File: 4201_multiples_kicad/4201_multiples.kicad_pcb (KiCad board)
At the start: 4 copper layers, 60 x 110 mm, 42 parts, among them J1 Conn_02x05_Odd_Even, J2 PJ398SM, J3 PJ398SM, J4 PJ398SM, J5 PJ398SM, J6 PJ398SM, J7 PJ398SM, J8 PJ398SM, J9 PJ398SM, U1 TL074, U2 TL074

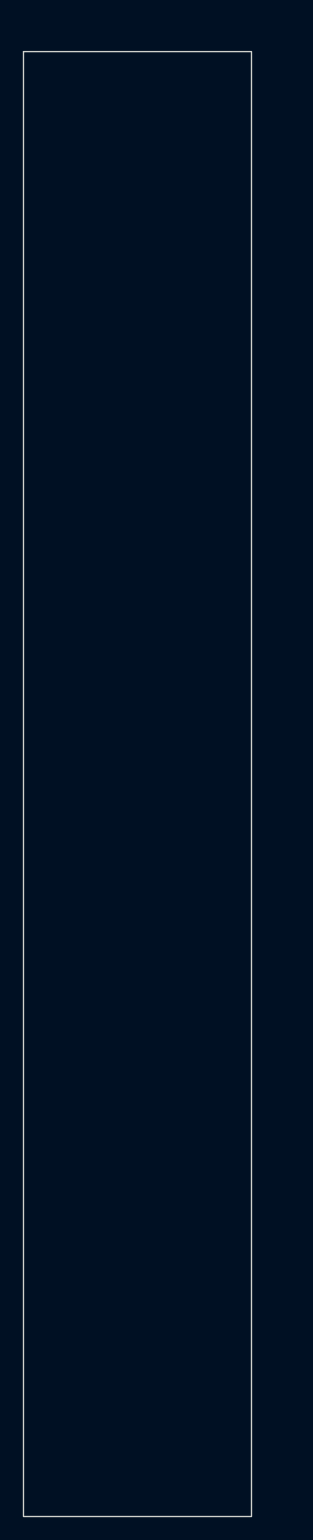
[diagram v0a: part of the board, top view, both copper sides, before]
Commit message: Add front panel silk footprint
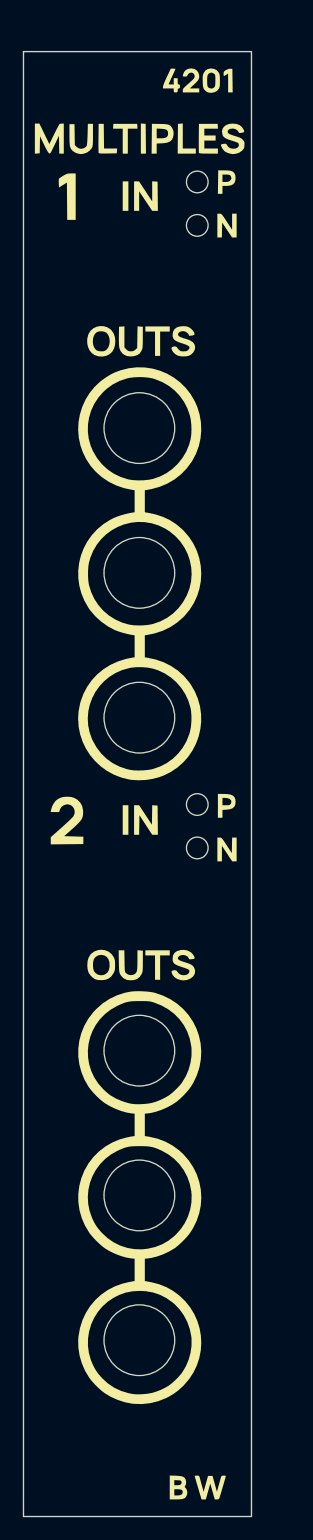
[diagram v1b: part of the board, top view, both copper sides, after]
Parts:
- added G***: LOGO, 4201_multiples:4204_multiples_panel_silk, F.Cu at (52.2, 41.5)
- added REF**: PJ392_Drill_Hole_Panel, OS_Drill_Holes:PJ392_Drill_Hole_Panel_D6.2mm, F.Cu at (50.2, 73.0)
- added REF**: Hole_1.9mm_LED, OS_Drill_Holes:LED_1.8mm_Drill_Hole_Panel_D1.9mm, F.Cu at (55.2, 55.2)
- added REF**: PJ392_Drill_Hole_Panel, OS_Drill_Holes:PJ392_Drill_Hole_Panel_D6.2mm, F.Cu at (50.2, 98.4)
- added REF**: Hole_1.9mm_LED, OS_Drill_Holes:LED_1.8mm_Drill_Hole_Panel_D1.9mm, F.Cu at (55.2, 51.4)
- added REF**: PJ392_Drill_Hole_Panel, OS_Drill_Holes:PJ392_Drill_Hole_Panel_D6.2mm, F.Cu at (50.2, 153.0)
- added REF**: PJ392_Drill_Hole_Panel, OS_Drill_Holes:PJ392_Drill_Hole_Panel_D6.2mm, F.Cu at (50.2, 127.6)
- added REF**: PJ392_Drill_Hole_Panel, OS_Drill_Holes:PJ392_Drill_Hole_Panel_D6.2mm, F.Cu at (50.2, 140.3)
- added REF**: PJ392_Drill_Hole_Panel, OS_Drill_Holes:PJ392_Drill_Hole_Panel_D6.2mm, F.Cu at (50.2, 85.7)
- added REF**: Hole_1.9mm_LED, OS_Drill_Holes:LED_1.8mm_Drill_Hole_Panel_D1.9mm, F.Cu at (55.2, 109.9)
- added REF**: Hole_1.9mm_LED, OS_Drill_Holes:LED_1.8mm_Drill_Hole_Panel_D1.9mm, F.Cu at (55.2, 106.0)

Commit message: Continue work on PCB layouts
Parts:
- removed the REF** at (50.2, 73.0)
- removed the REF** at (55.2, 55.2)
- removed the REF** at (50.2, 98.4)
- removed the REF** at (55.2, 51.4)
- removed the REF** at (50.2, 153.0)
- removed the REF** at (50.2, 127.6)
- removed the REF** at (50.2, 140.3)
- removed the REF** at (50.2, 85.7)
- removed the REF** at (55.2, 109.9)
- removed the REF** at (55.2, 106.0)
- added J10: Conn_01x03_Female, Connector_PinSocket_2.54mm:PinSocket_1x03_P2.54mm_Vertical, B.Cu at (98.4, 62.2)
- added J11: Conn_01x04_Female, Connector_PinSocket_2.54mm:PinSocket_1x04_P2.54mm_Vertical, B.Cu at (83.2, 149.9)
- added J12: Conn_01x03_Female, Connector_PinSocket_2.54mm:PinSocket_1x03_P2.54mm_Vertical, B.Cu at (98.4, 144.8)
- added J13: Conn_01x05_Male, Connector_PinHeader_2.54mm:PinHeader_1x05_P2.54mm_Vertical, F.Cu at (123.2, 52.1)
- added J14: Conn_01x03_Male, Connector_PinHeader_2.54mm:PinHeader_1x03_P2.54mm_Vertical, F.Cu at (138.4, 62.2)
- added J15: Conn_01x04_Male, Connector_PinHeader_2.54mm:PinHeader_1x04_P2.54mm_Vertical, F.Cu at (123.2, 149.9)
- added J16: Conn_01x03_Male, Connector_PinHeader_2.54mm:PinHeader_1x03_P2.54mm_Vertical, F.Cu at (138.4, 144.8)
- added J17: Conn_02x05_Odd_Even, Connector_IDC:IDC-Header_2x05_P2.54mm_Vertical, B.Cu at (125.6, 111.1)
- added REF**: PJ392_Drill_Hole_Panel, OS_Drill_Holes:PJ392_Drill_Hole_Panel_D6.2mm, F.Cu at (50.8, 73.7)
- added REF**: Hole_M2.5_2.7mm, OS_Drill_Holes:M3_Drill_Hole_D3.2mm, F.Cu at (90.8, 92.7)
- added REF**: PJ392_Drill_Hole_Panel, OS_Drill_Holes:PJ392_Drill_Hole_Panel_D6.2mm, F.Cu at (50.8, 114.3)
- added REF**: Hole_1.9mm_LED, OS_Drill_Holes:LED_1.8mm_Drill_Hole_Panel_D1.9mm, F.Cu at (55.9, 106.7)
- added REF**: PJ392_Drill_Hole_Panel, OS_Drill_Holes:PJ392_Drill_Hole_Panel_D6.2mm, F.Cu at (50.8, 128.3)
- added REF**: Hole_1.9mm_LED, OS_Drill_Holes:LED_1.8mm_Drill_Hole_Panel_D1.9mm, F.Cu at (55.9, 110.5)
- added REF**: PJ392_Drill_Hole_Panel, OS_Drill_Holes:PJ392_Drill_Hole_Panel_D6.2mm, F.Cu at (50.8, 153.7)
- added REF**: Hole_1.9mm_LED, OS_Drill_Holes:LED_1.8mm_Drill_Hole_Panel_D1.9mm, F.Cu at (55.9, 52.1)
- added REF**: PJ392_Drill_Hole_Panel, OS_Drill_Holes:PJ392_Drill_Hole_Panel_D6.2mm, F.Cu at (50.8, 59.7)
- added REF**: PJ392_Drill_Hole_Panel, OS_Drill_Holes:PJ392_Drill_Hole_Panel_D6.2mm, F.Cu at (50.8, 141.0)
- added REF**: PJ392_Drill_Hole_Panel, OS_Drill_Holes:PJ392_Drill_Hole_Panel_D6.2mm, F.Cu at (50.8, 99.1)
- added REF**: Hole_M2.5_2.7mm, OS_Drill_Holes:M3_Drill_Hole_D3.2mm, F.Cu at (130.8, 92.7)
- added REF**: Hole_1.9mm_LED, OS_Drill_Holes:LED_1.8mm_Drill_Hole_Panel_D1.9mm, F.Cu at (55.9, 55.9)
- added REF**: PJ392_Drill_Hole_Panel, OS_Drill_Holes:PJ392_Drill_Hole_Panel_D6.2mm, F.Cu at (50.8, 86.4)
- C1, C2: moved to B.Cu
- D1, D3: value 1N4148 -> 1.8mm_green; footprint Diode_SMD:D_1206_3216Metric_Pad1.42x1.75mm_HandSolder -> LED_THT:LED_D1.8mm_W3.3mm_H2.4mm
- D10, D12: value 1.8mm_red -> 1N4148; footprint LED_THT:LED_D1.8mm_W3.3mm_H2.4mm -> Diode_SMD:D_1206_3216Metric_Pad1.42x1.75mm_HandSolder
- D11, D9: value 1.8mm_green -> 1N4148; footprint LED_THT:LED_D1.8mm_W3.3mm_H2.4mm -> Diode_SMD:D_1206_3216Metric_Pad1.42x1.75mm_HandSolder
- D2, D4: value 1N4148 -> 1.8mm_red; footprint Diode_SMD:D_1206_3216Metric_Pad1.42x1.75mm_HandSolder -> LED_THT:LED_D1.8mm_W3.3mm_H2.4mm
- J1: value Conn_02x05_Odd_Even -> AudioJack2; footprint Connector_IDC:IDC-Header_2x05_P2.54mm_Vertical -> OS_Connectors:Jack_3.5mm_PJ392_Vertical
- J2, J3, J4, J5, J6, J7, J8: value PJ398SM -> AudioJack2; footprint 4ms_Jack:EighthInch_PJ398SM -> OS_Connectors:Jack_3.5mm_PJ392_Vertical
- J9: value PJ398SM -> Conn_01x05_Female; footprint 4ms_Jack:EighthInch_PJ398SM -> Connector_PinSocket_2.54mm:PinSocket_1x05_P2.54mm_Vertical; moved to B.Cu
- R10, R12: value 4k7 -> 100R
- R11: value 39k -> 100R
- R2: value 220k -> 39k
- R3: value 100R -> 4k7
- R7: value 100R -> 220k
- R8: value 100R -> 39k
- R9: value 39k -> 4k7
- moved J7 187.8 mm to (90.8, 141.0)
- moved J8 173.8 mm to (90.8, 153.7)
- moved D3 167.1 mm to (94.6, 106.7)
- moved D10 165.7 mm to (134.0, 147.3)
- moved J5 161.2 mm to (90.8, 114.3)
- moved R9 158.6 mm to (145.4, 156.8)
- moved D1 154.7 mm to (94.6, 52.1)
- moved R12 152.9 mm to (149.2, 123.2), turned to 90 degrees
- moved J4 149.7 mm to (90.8, 99.1)
- moved D9 145.2 mm to (134.0, 144.8), turned to 180 degrees
- moved C2 144.8 mm to (136.5, 112.4), turned to -90 degrees
- moved D11 142.0 mm to (151.1, 154.3), turned to 180 degrees
- moved D4 140.3 mm to (97.2, 110.5), turned to 180 degrees
- moved D2 139.2 mm to (97.2, 55.9), turned to 180 degrees
- moved D12 135.0 mm to (151.1, 156.8)
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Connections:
- D1 pad 1: Net-(D1-Pad1) -> /interface/LED_1_PK_NA
- D1 pad 2: /U1D_FBK -> /interface/LED_1P_A
- D10 pad 1: Net-(D2-Pad2) -> /main_board/U2D_FBK
- D10 pad 2: /U1D_OUT -> /main_board/LED_2N_K
- D11 pad 1: /U2D_OUT -> GND
- D11 pad 2: Net-(D5-Pad1) -> Net-(D11-Pad2)
- D12 pad 1: Net-(D6-Pad2) -> Net-(D12-Pad1)
- D12 pad 2: /U2D_OUT -> GND
- D2 pad 1: /U1D_FBK -> /interface/LED_1N_K
- D2 pad 2: Net-(D2-Pad2) -> /interface/LED_1_PK_NA
- D3 pad 1: GND -> /interface/LED_2_PK_NA
- D3 pad 2: Net-(D3-Pad2) -> /interface/LED_2P_A
- D4 pad 1: Net-(D4-Pad1) -> /interface/LED_2N_K
- D4 pad 2: GND -> /interface/LED_2_PK_NA
- D5 pad 1: Net-(D5-Pad1) -> /main_board/LED_1P_A
- D5 pad 2: /U2D_FBK -> /main_board/U1D_FBK
- D6 pad 1: /U2D_FBK -> /main_board/U1D_FBK
- D6 pad 2: Net-(D6-Pad2) -> /main_board/LED_1N_K
- D9 pad 1: /U1D_OUT -> /main_board/LED_2P_A
- D9 pad 2: Net-(D1-Pad1) -> /main_board/U2D_FBK
- J9 pad 1: /OUT_2_3 -> /interface/IN_1
- J9 pad 2: GND -> /interface/OUT_1_1
- J9 pad 3: unconnected-(J9-Pad3) -> /interface/OUT_1_2
- R1 pad 2: /IN_1 -> /main_board/IN_1
- R10 pad 1: /U1D_FBK -> /main_board/U2A_OUT
- R10 pad 2: Net-(D4-Pad1) -> /main_board/OUT_2_1
- R11 pad 1: /U2D_FBK -> /main_board/U2B_OUT
- R11 pad 2: Net-(D7-Pad2) -> /main_board/OUT_2_2
- R12 pad 1: /U2D_FBK -> /main_board/U2C_OUT
- R12 pad 2: Net-(D8-Pad1) -> /main_board/OUT_2_3
- R2 pad 1: GND -> /main_board/U1D_FBK
- R2 pad 2: /IN_2 -> Net-(D7-Pad2)
- R3 pad 1: /U1A_OUT -> /main_board/U1D_FBK
- R3 pad 2: /OUT_1_1 -> Net-(D8-Pad1)
- R4 pad 1: /U1B_OUT -> /main_board/U1A_OUT
- R4 pad 2: /OUT_1_2 -> /main_board/OUT_1_1
- R5 pad 1: /U1C_OUT -> /main_board/U1B_OUT
- R5 pad 2: /OUT_1_3 -> /main_board/OUT_1_2
- R6 pad 1: /U2A_OUT -> /main_board/U1C_OUT
- R6 pad 2: /OUT_2_1 -> /main_board/OUT_1_3
- R7 pad 1: /U2B_OUT -> GND
- R7 pad 2: /OUT_2_2 -> /main_board/IN_2
- R8 pad 1: /U2C_OUT -> /main_board/U2D_FBK
- R8 pad 2: /OUT_2_3 -> Net-(D11-Pad2)
- R9 pad 1: /U1D_FBK -> /main_board/U2D_FBK
- R9 pad 2: Net-(D3-Pad2) -> Net-(D12-Pad1)
- U1 pad 1: /U1A_OUT -> /main_board/U1A_OUT
- U1 pad 10: /IN_1 -> /main_board/IN_1
- U1 pad 12: /IN_1 -> /main_board/IN_1
- U1 pad 13: /U1D_FBK -> /main_board/U1D_FBK
- U1 pad 14: /U1D_OUT -> /main_board/LED_1_PK_NA
- U1 pad 2: /U1A_OUT -> /main_board/U1A_OUT
- U1 pad 3: /IN_1 -> /main_board/IN_1
- U1 pad 5: /IN_1 -> /main_board/IN_1
- U1 pad 6: /U1B_OUT -> /main_board/U1B_OUT
- U1 pad 7: /U1B_OUT -> /main_board/U1B_OUT
- U1 pad 8: /U1C_OUT -> /main_board/U1C_OUT
- U1 pad 9: /U1C_OUT -> /main_board/U1C_OUT
- U2 pad 1: /U2A_OUT -> /main_board/U2A_OUT
- U2 pad 10: /IN_2 -> /main_board/IN_2
- U2 pad 12: /IN_2 -> /main_board/IN_2
- U2 pad 13: /U2D_FBK -> /main_board/U2D_FBK
- U2 pad 14: /U2D_OUT -> /main_board/LED_2_PK_NA
- U2 pad 2: /U2A_OUT -> /main_board/U2A_OUT
- U2 pad 3: /IN_2 -> /main_board/IN_2
- U2 pad 5: /IN_2 -> /main_board/IN_2
- U2 pad 6: /U2B_OUT -> /main_board/U2B_OUT
- U2 pad 7: /U2B_OUT -> /main_board/U2B_OUT
- U2 pad 8: /U2C_OUT -> /main_board/U2C_OUT
- U2 pad 9: /U2C_OUT -> /main_board/U2C_OUT
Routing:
- added copper zone on In1.Cu, net /interface/0V
- added copper zone on In2.Cu, net /interface/0V
- added copper zone on In1.Cu, net GND
- added copper zone on In2.Cu, net GND

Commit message: Layout components
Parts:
- added REF**: PinHeader_1x04_P2.54mm_Vertical, Connector_PinHeader_2.54mm:PinHeader_1x04_P2.54mm_Vertical, F.Cu at (126.9, 121.3)
- added REF**: PinSocket_1x04_P2.54mm_Vertical, Connector_PinSocket_2.54mm:PinSocket_1x04_P2.54mm_Vertical, B.Cu at (86.9, 121.3)
- C3, C4, C5, C6, D10, D11, D12, D5, D6, D7, D8, D9, R1, R10, R11, R12, R2, R3, R4, R5, R6, R7, R8, R9, U1, U2: moved to B.Cu
- moved R10 36.7 mm to (126.4, 138.4), turned to -90 degrees
- moved R6 36.2 mm to (128.9, 87.0), turned to 180 degrees
- moved C4 35.9 mm to (124.5, 81.3), turned to -90 degrees
- moved R7 33.1 mm to (130.8, 138.4), turned to 90 degrees
- moved R11 30.7 mm to (135.3, 138.4), turned to -90 degrees
- moved C5 30.5 mm to (124.5, 131.4), turned to 90 degrees
- moved R5 29.0 mm to (126.4, 74.3), turned to -90 degrees
- moved U1 28.6 mm to (130.8, 81.3), turned to 90 degrees
- moved U2 24.8 mm to (130.8, 131.4), turned to -90 degrees
- moved R1 22.9 mm to (130.8, 74.3), turned to -90 degrees
- moved C3 22.7 mm to (137.2, 81.3), turned to -90 degrees
- moved C6 21.5 mm to (137.2, 131.4), turned to 90 degrees
- moved R4 17.9 mm to (135.3, 74.3), turned to 90 degrees
- moved D11 16.4 mm to (134.7, 153.9)
- moved R8 16.4 mm to (129.0, 153.9)
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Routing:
- removed copper zone on In1.Cu, net /interface/0V
- removed copper zone on In2.Cu, net /interface/0V
- removed copper zone on In1.Cu, net GND
- removed copper zone on In2.Cu, net GND
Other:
- copper layers 4 -> 2

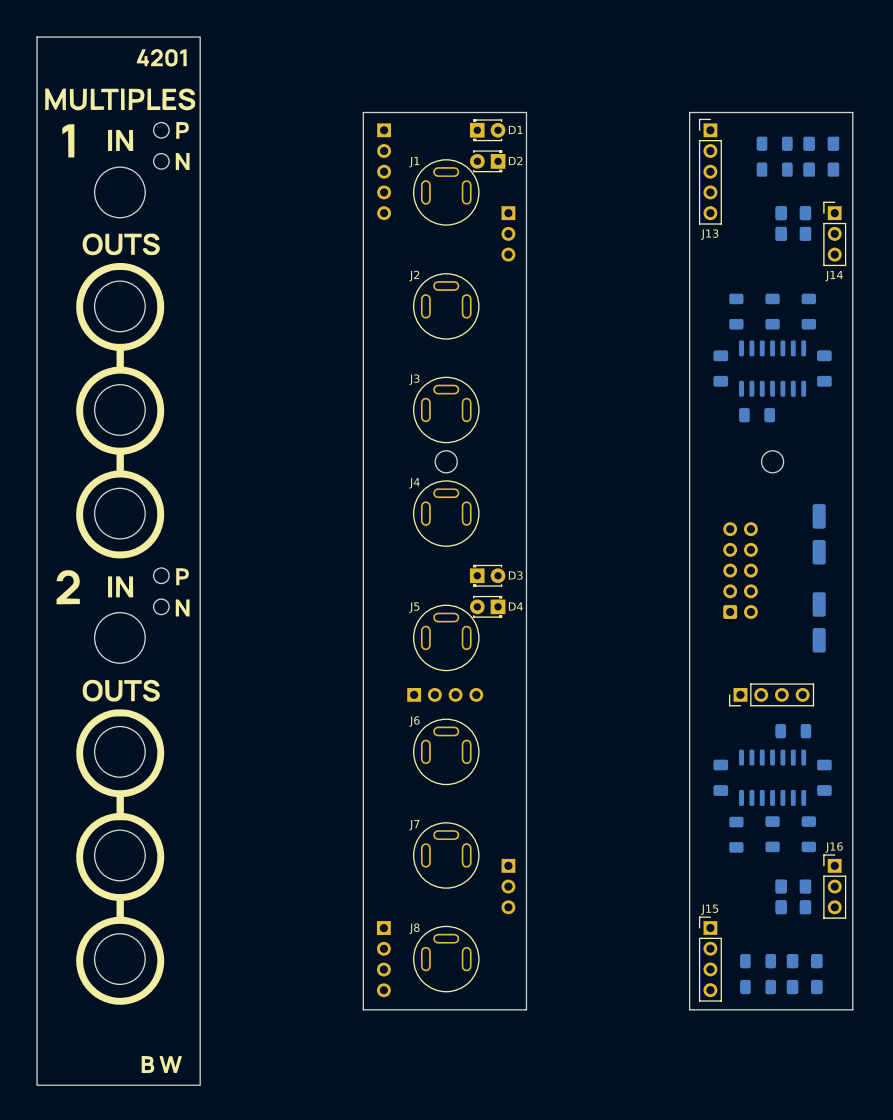
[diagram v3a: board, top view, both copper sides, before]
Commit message: Finish layout first draft
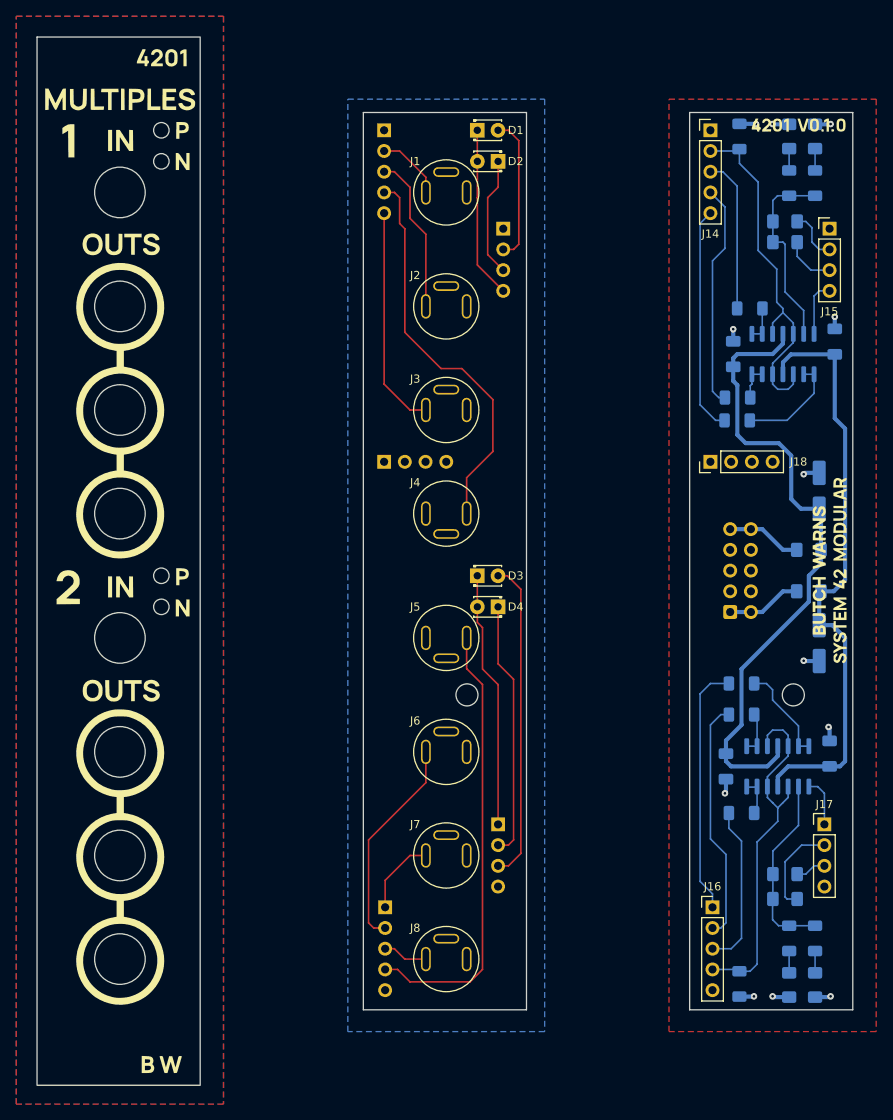
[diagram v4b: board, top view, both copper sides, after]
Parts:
- removed the J14 at (138.4, 62.2)
- removed the REF** at (126.9, 121.3)
- removed the REF** at (90.8, 92.7)
- removed the REF** at (86.9, 121.3)
- removed the REF** at (130.8, 92.7)
- added D13: 1N5817, Diode_SMD:D_1206_3216Metric_Pad1.42x1.75mm_HandSolder, B.Cu at (135.3, 103.5)
- added D14: 1N5817, Diode_SMD:D_1206_3216Metric_Pad1.42x1.75mm_HandSolder, B.Cu at (135.3, 108.6)
- added G***: LOGO, 4201_multiples:BUTCH_WARNS, F.Cu at (136.5, 106.0)
- added G***: LOGO, 4201_multiples:SYSTEM_42_MOUDULAR, F.Cu at (139.1, 106.0)
- added G***: LOGO, 4201_multiples:4201_V_0_1_0, F.Cu at (134.0, 51.4)
- added G***: LOGO, 4201_multiples:BUTCHWARNS_DE, B.Cu at (130.6, 90.2)
- added J13: Conn_01x04_Female, Connector_PinSocket_2.54mm:PinSocket_1x04_P2.54mm_Vertical, B.Cu at (83.2, 92.7)
- added J17: Conn_01x04_Male, Connector_PinHeader_2.54mm:PinHeader_1x04_P2.54mm_Vertical, F.Cu at (137.2, 137.2)
- added J18: Conn_01x04_Male, Connector_PinHeader_2.54mm:PinHeader_1x04_P2.54mm_Vertical, F.Cu at (123.2, 92.7)
- added REF**: M2.5_Drill_Hole_2.7mm, OS_Drill_Holes:LED_3mm_Drill_Hole_Panel_D3.0mm, F.Cu at (133.3, 121.3)
- added REF**: M2.5_Drill_Hole_2.7mm, OS_Drill_Holes:LED_3mm_Drill_Hole_Panel_D3.0mm, F.Cu at (93.3, 121.3)
- J10, J12: value Conn_01x03_Female -> Conn_01x04_Female; footprint Connector_PinSocket_2.54mm:PinSocket_1x03_P2.54mm_Vertical -> Connector_PinSocket_2.54mm:PinSocket_1x04_P2.54mm_Vertical
- J11: value Conn_01x04_Female -> Conn_01x05_Female; footprint Connector_PinSocket_2.54mm:PinSocket_1x04_P2.54mm_Vertical -> Connector_PinSocket_2.54mm:PinSocket_1x05_P2.54mm_Vertical
- J16: value Conn_01x03_Male -> Conn_01x05_Male; footprint Connector_PinHeader_2.54mm:PinHeader_1x03_P2.54mm_Vertical -> Connector_PinHeader_2.54mm:PinHeader_1x05_P2.54mm_Vertical
- moved J15 87.0 mm to (137.8, 64.1)
- moved R1 21.8 mm to (126.7, 52.8)
- moved R11 20.2 mm to (127.0, 119.9), turned to 180 degrees
- moved R7 18.8 mm to (126.7, 156.7)
- moved J16 15.8 mm to (123.4, 147.3)
- moved R10 14.7 mm to (127.0, 123.7), turned to 180 degrees
- moved C4 14.4 mm to (138.4, 78.0)
- moved R5 13.3 mm to (126.5, 87.6), turned to 180 degrees
- moved R12 11.9 mm to (127.0, 135.8), turned to 180 degrees
- moved C3 11.3 mm to (126.0, 79.5), turned to 90 degrees
- moved R8 7.52 mm to (136.0, 151.1), turned to -90 degrees
- moved R4 7.25 mm to (128.0, 73.9), turned to 180 degrees
- moved R9 7.08 mm to (132.8, 151.1), turned to -90 degrees
- moved C1 5.33 mm to (136.5, 96.3), turned to 90 degrees
- moved J12 5.24 mm to (97.2, 137.2)
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- renumbered J13 to J14, J17 to J19
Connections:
- net /main_board/U1A_OUT renamed Net-(R4-Pad1)
- net /main_board/U2A_OUT renamed Net-(R10-Pad1)
- net /main_board/U2B_OUT renamed Net-(R11-Pad1)
- D10 pad 1: /main_board/U2D_FBK -> Net-(D10-Pad1)
- D5 pad 2: /main_board/U1D_FBK -> Net-(D5-Pad2)
- D6 pad 1: /main_board/U1D_FBK -> Net-(D5-Pad2)
- D9 pad 2: /main_board/U2D_FBK -> Net-(D10-Pad1)
- J10 pad 1: /interface/LED_1P_A -> /interface/0V
- J10 pad 2: /interface/LED_1N_K -> /interface/LED_1P_A
- J10 pad 3: /interface/LED_1_PK_NA -> /interface/LED_1N_K
- J11 pad 1: /interface/IN_2 -> /interface/OUT_2_2
- J11 pad 3: /interface/OUT_2_2 -> /interface/OUT_2_3
- J11 pad 4: /interface/OUT_2_3 -> /interface/IN_2
- J12 pad 1: /interface/LED_2P_A -> /interface/LED_2_PK_NA
- J12 pad 3: /interface/LED_2_PK_NA -> /interface/LED_2P_A
- J14 pad 1: /main_board/IN_1 -> GND
- J14 pad 2: /main_board/OUT_1_1 -> /main_board/IN_1
- J14 pad 3: /main_board/OUT_1_2 -> /main_board/OUT_1_1
- J14 pad 5: GND -> /main_board/OUT_1_2
- J15 pad 1: /main_board/IN_2 -> GND
- J15 pad 2: /main_board/OUT_2_1 -> /main_board/LED_1P_A
- J15 pad 3: /main_board/OUT_2_2 -> /main_board/LED_1N_K
- J15 pad 4: /main_board/OUT_2_3 -> /main_board/LED_1_PK_NA
- J16 pad 1: /main_board/LED_2P_A -> /main_board/OUT_2_2
- J16 pad 2: /main_board/LED_2N_K -> /main_board/OUT_2_1
- J16 pad 3: /main_board/LED_2_PK_NA -> /main_board/OUT_2_3
- J19 pad 1: -12V -> /main_board/-12V_preD
- J19 pad 10: +12V -> /main_board/+12V_preD
- J19 pad 2: -12V -> /main_board/-12V_preD
- J19 pad 9: +12V -> /main_board/+12V_preD
- J9 pad 1: /interface/IN_1 -> /interface/0V
- J9 pad 2: /interface/OUT_1_1 -> /interface/IN_1
- J9 pad 3: /interface/OUT_1_2 -> /interface/OUT_1_1
- J9 pad 5: /interface/0V -> /interface/OUT_1_2
- R12 pad 1: /main_board/U2C_OUT -> Net-(R12-Pad1)
- R2 pad 1: /main_board/U1D_FBK -> Net-(D5-Pad2)
- R3 pad 1: /main_board/U1D_FBK -> Net-(D5-Pad2)
- R5 pad 1: /main_board/U1B_OUT -> Net-(R5-Pad1)
- R6 pad 1: /main_board/U1C_OUT -> Net-(R6-Pad1)
- R8 pad 1: /main_board/U2D_FBK -> Net-(D10-Pad1)
- R9 pad 1: /main_board/U2D_FBK -> Net-(D10-Pad1)
- U1 pad 13: /main_board/U1D_FBK -> Net-(R6-Pad1)
- U1 pad 14: /main_board/LED_1_PK_NA -> Net-(R6-Pad1)
- U1 pad 6: /main_board/U1B_OUT -> Net-(D5-Pad2)
- U1 pad 7: /main_board/U1B_OUT -> /main_board/LED_1_PK_NA
- U1 pad 8: /main_board/U1C_OUT -> Net-(R5-Pad1)
- U1 pad 9: /main_board/U1C_OUT -> Net-(R5-Pad1)
- U2 pad 13: /main_board/U2D_FBK -> Net-(R12-Pad1)
- U2 pad 14: /main_board/LED_2_PK_NA -> Net-(R12-Pad1)
- U2 pad 8: /main_board/U2C_OUT -> /main_board/LED_2_PK_NA
- U2 pad 9: /main_board/U2C_OUT -> Net-(D10-Pad1)
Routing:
- net +12V: track 0.00 -> 78.5 mm
- net -12V: track 0.00 -> 73.3 mm
- net /interface/IN_2: track 0.00 -> 54.6 mm
- net /interface/OUT_1_3: track 0.00 -> 48.5 mm
- net /main_board/IN_2: track 0.00 -> 44.1 mm
- net /main_board/IN_1: track 0.00 -> 43.6 mm
- net /interface/LED_2P_A: track 0.00 -> 39.3 mm
- net /interface/LED_2_PK_NA: track 0.00 -> 31.5 mm
- net /interface/LED_2N_K: track 0.00 -> 31.5 mm
- net /main_board/OUT_2_2: track 0.00 -> 30.8 mm
- net /main_board/OUT_2_1: track 0.00 -> 29.7 mm
- net /main_board/OUT_1_2: track 0.00 -> 27.8 mm
- net /main_board/OUT_1_3: track 0.00 -> 27.6 mm
- net /interface/OUT_1_2: track 0.00 -> 27.4 mm
- net /interface/OUT_2_1: track 0.00 -> 26.0 mm
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- added copper zone on B.Cu, net /interface/0V
- added copper zone on B.Cu, net GND
- added copper zone on F.Cu, net GND
